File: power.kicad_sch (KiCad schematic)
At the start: 40 parts, among them T1 net-tie, U2 TPS546D24ARVFR

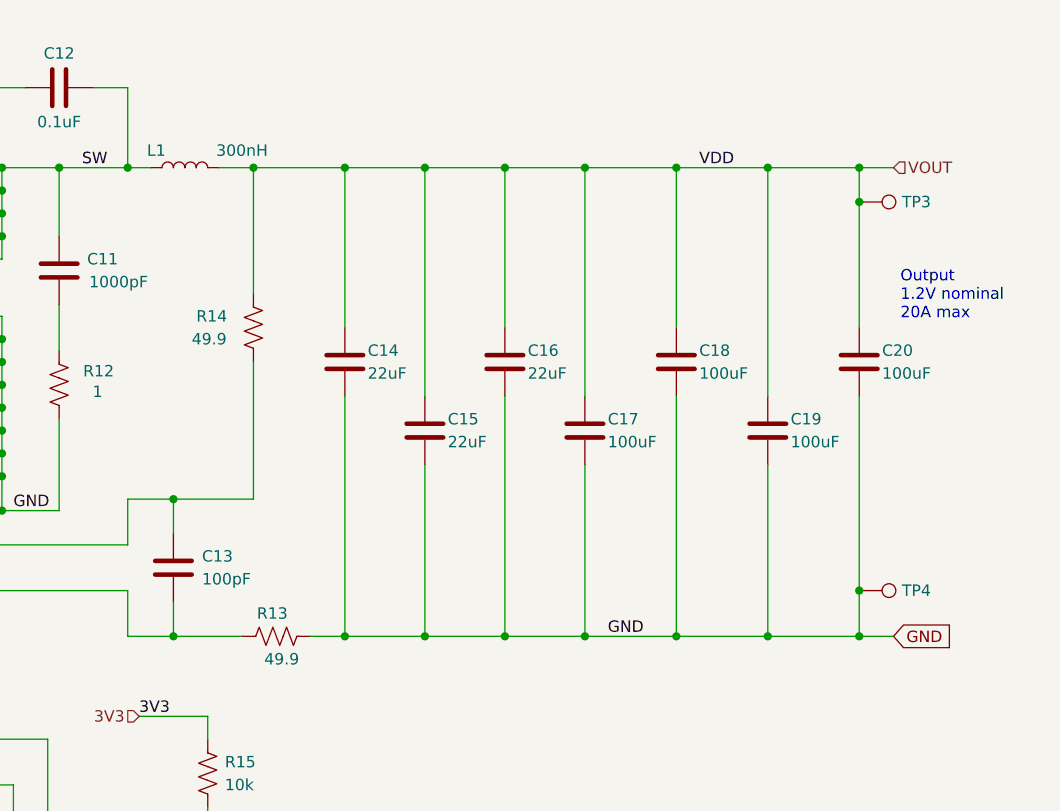
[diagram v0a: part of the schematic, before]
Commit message: use global GND level provided by default with KiCad and remove custom global GND
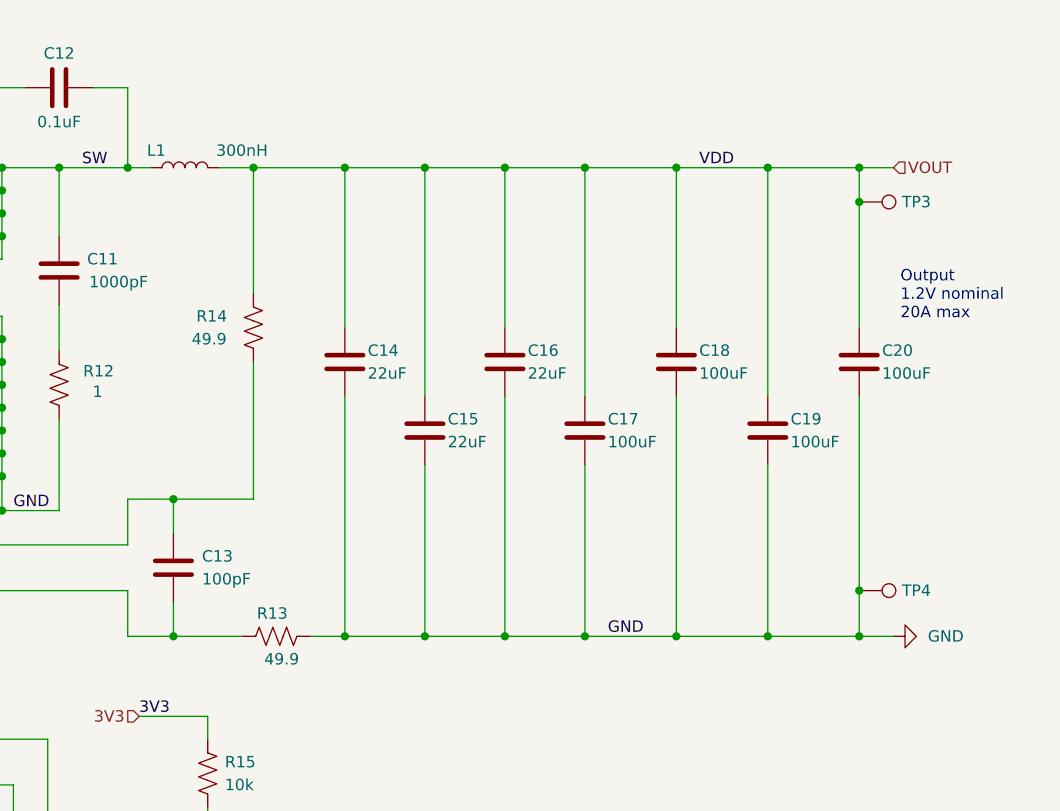
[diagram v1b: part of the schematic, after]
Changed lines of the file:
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@@
 (kicad_sch
-	(version 20231120)
+	(version 20250114)
 	(generator "eeschema")
-	(generator_version "8.0")
+	(generator_version "9.0")
 	(paper "A")
 	(title_block
@@
 		(rev "207")
 	)
+	(text "TPS546D24A is a Buck regulator that steps 4.5-5.5V down to 1.2V @ 20A for the BM1368"
+		(exclude_from_sim no)
+		(at 111.76 17.78 0)
+		(effects
+			(font
+				(size 1.27 1.27)
+			)
+			(justify left bottom)
+		)
+	)
+	(text "https://webench.ti.com/appinfo/webench/scripts/SDP.cgi?ID=3808DBEB40D18F5D"
+		(exclude_from_sim no)
+		(at 152.908 19.304 0)
+		(effects
+			(font
+				(size 1.27 1.27)
+			)
+		)
+	)
+	(text "Input \n4.5-5.5V"
+		(exclude_from_sim no)
+		(at 25.908 28.448 0)
+		(effects
+			(font
+				(size 1.27 1.27)
+			)
+			(justify left bottom)
+		)
+	)
+	(text "PGD is an open drain output\nfrom the TPS546D24. Pull up to 3.3V"
+		(exclude_from_sim no)
+		(at 151.13 120.65 0)
+		(effects
+			(font
+				(size 1.27 1.27)
+			)
+			(justify left bottom)
+		)
+	)
+	(text "I2C ADDR = 0x24"
+		(exclude_from_sim no)
+		(at 85.344 91.186 0)
+		(effects
+			(font
+				(size 1.27 1.27)
+			)
+			(justify left bottom)
+		)
+	)
+	(text "Output \n1.2V nominal\n20A max"
+		(exclude_from_sim no)
+		(at 239.522 56.388 0)
+		(effects
+			(font
+				(size 1.27 1.27)
+			)
+			(justify left bottom)
+		)
+	)
+	(text "Connect at\nU3 Pin 37"
+		(exclude_from_sim no)
+		(at 115.57 148.59 0)
+		(effects
+			(font
+				(size 1.27 1.27)
+			)
+			(justify left bottom)
+		)
+	)
 	(junction
 		(at 66.04 90.17)
@@
 		)
 	)
-	(text "TPS546D24A is a Buck regulator that steps 4.5-5.5V down to 1.2V @ 20A for the BM1368"
-		(exclude_from_sim no)
-		(at 111.76 17.78 0)
-		(effects
-			(font
-				(size 1.27 1.27)
-			)
-			(justify left bottom)
-		)
-	)
-	(text "https://webench.ti.com/appinfo/webench/scripts/SDP.cgi?ID=3808DBEB40D18F5D"
-		(exclude_from_sim no)
-		(at 152.908 19.304 0)
-		(effects
-			(font
-				(size 1.27 1.27)
-			)
-		)
-	)
-	(text "Input \n4.5-5.5V"
-		(exclude_from_sim no)
-		(at 25.908 28.448 0)
-		(effects
-			(font
-				(size 1.27 1.27)
-			)
-			(justify left bottom)
-		)
-	)
-	(text "PGD is an open drain output\nfrom the TPS546D24. Pull up to 3.3V"
-		(exclude_from_sim no)
-		(at 151.13 120.65 0)
-		(effects
-			(font
-				(size 1.27 1.27)
-			)
-			(justify left bottom)
-		)
-	)
-	(text "I2C ADDR = 0x24"
-		(exclude_from_sim no)
-		(at 85.344 91.186 0)
-		(effects
-			(font
-				(size 1.27 1.27)
-			)
-			(justify left bottom)
-		)
-	)
-	(text "Output \n1.2V nominal\n20A max"
-		(exclude_from_sim no)
-		(at 239.522 56.388 0)
-		(effects
-			(font
-				(size 1.27 1.27)
-			)
-			(justify left bottom)
-		)
-	)
-	(text "Connect at\nU3 Pin 37"
-		(exclude_from_sim no)
-		(at 115.57 148.59 0)
-		(effects
-			(font
-				(size 1.27 1.27)
-			)
-			(justify left bottom)
-		)
-	)
 	(label "GND"
 		(at 134.62 140.97 180)
-		(fields_autoplaced yes)
 		(effects
 			(font
@@
 	(label "PMB_SDA"
 		(at 99.06 101.6 0)
-		(fields_autoplaced yes)
 		(effects
 			(font
@@
 	(label "GND"
 		(at 96.52 74.93 0)
-		(fields_autoplaced yes)
 		(effects
 			(font
@@
 	(label "SW"
 		(at 148.59 39.37 0)
-		(fields_autoplaced yes)
 		(effects
 			(font
@@
 	(label "GND"
 		(at 140.97 77.47 0)
-		(fields_autoplaced yes)
 		(effects
 			(font
@@
 	(label "PMB_SCL"
 		(at 99.06 104.14 0)
-		(fields_autoplaced yes)
 		(effects
 			(font
@@
 	(label "AGND"
 		(at 118.11 128.27 180)
-		(fields_autoplaced yes)
 		(effects
 			(font
@@
 	(label "AGND"
 		(at 72.39 72.39 0)
-		(fields_autoplaced yes)
 		(effects
 			(font
@@
 	(label "GND"
 		(at 207.01 91.44 0)
-		(fields_autoplaced yes)
 		(effects
 			(font
@@
 	(label "PMB_ALRT"
 		(at 99.06 106.68 0)
-		(fields_autoplaced yes)
 		(effects
 			(font
@@
 	(label "PGOOD"
 		(at 147.32 114.3 0)
-		(fields_autoplaced yes)
 		(effects
 			(font
@@
 	(label "GND"
 		(at 63.5 34.29 0)
-		(fields_autoplaced yes)
 		(effects
 			(font
@@
 	(label "AGND"
 		(at 109.22 140.97 0)
-		(fields_autoplaced yes)
 		(effects
 			(font
@@
 	(label "VIN"
 		(at 35.56 17.78 0)
-		(fields_autoplaced yes)
 		(effects
 			(font
@@
 	(label "VDD"
 		(at 217.17 39.37 0)
-		(fields_autoplaced yes)
 		(effects
 			(font
@@
 	(label "3V3"
 		(at 154.94 100.33 0)
-		(fields_autoplaced yes)
 		(effects
 			(font
@@
 		)
 	)
-	(global_label "GND"
-		(shape input)
-		(at 238.76 91.44 0)
-		(fields_autoplaced yes)
-		(effects
-			(font
-				(size 1.27 1.27)
-			)
-			(justify left)
-		)
-		(property "Intersheetrefs" "${INTERSHEET_REFS}"
-			(at 245.6157 91.44 0)
-			(effects
-				(font
-					(size 1.27 1.27)
-				)
-				(justify left)
-				(hide yes)
-			)
-		)
-	)
 	(hierarchical_label "VOUT"
 		(shape input)
 		(at 238.76 39.37 0)
-		(fields_autoplaced yes)
 		(effects
 			(font
@@
 		(shape output)
 		(at 99.06 106.68 180)
-		(fields_autoplaced yes)
 		(effects
 			(font
@@
 		(shape input)
 		(at 154.94 100.33 180)
-		(fields_autoplaced yes)
 		(effects
 			(font
@@
 		(shape input)
 		(at 99.06 104.14 180)
-		(fields_autoplaced yes)
 		(effects
 			(font
@@
 		(shape output)
 		(at 172.72 114.3 0)
-		(fields_autoplaced yes)
 		(effects
 			(font
@@
 		(shape input)
 		(at 99.06 101.6 180)
-		(fields_autoplaced yes)
 		(effects
 			(font
@@
 		(shape output)
 		(at 102.87 17.78 0)
-		(fields_autoplaced yes)
 		(effects
 			(font
@@
 		(shape input)
 		(at 34.29 17.78 180)
-		(fields_autoplaced yes)
 		(effects
 			(font
@@
 	)
 	(symbol
+		(lib_id "power:GND")
+		(at 238.76 91.44 90)
+		(mirror x)
+		(unit 1)
+		(exclude_from_sim no)
+		(in_bom yes)
+		(on_board yes)
+		(dnp no)
+		(property "Reference" "#PWR04"
+			(at 245.11 91.44 0)
+			(effects
+				(font
+					(size 1.27 1.27)
+				)
+				(hide yes)
+			)
+		)
+		(property "Value" "GND"
+			(at 242.57 91.4399 90)
+			(effects
+				(font
+					(size 1.27 1.27)
+				)
+				(justify right)
+			)
+		)
+		(property "Footprint" ""
+			(at 238.76 91.44 0)
+			(effects
+				(font
+					(size 1.27 1.27)
+				)
+				(hide yes)
+			)
+		)
+		(property "Datasheet" ""
+			(at 238.76 91.44 0)
+			(effects
+				(font
+					(size 1.27 1.27)
+				)
+				(hide yes)
+			)
+		)
+		(property "Description" "Power symbol creates a global label with name \"GND\" , ground"
+			(at 238.76 91.44 0)
+			(effects
+				(font
+					(size 1.27 1.27)
+				)
+				(hide yes)
+			)
+		)
+		(pin "1"
+		)
+		(instances
+			(project "bitaxeUltra"
+				(path "/e63e39d7-6ac0-4ffd-8aa3-1841a4541b55/8ec0a9c6-2b78-44ef-a83d-9047d2828409"
+					(reference "#PWR04")
+					(unit 1)
+				)
+			)
+		)
+	)
+	(symbol
 		(lib_id "Device:R_US")
 		(at 92.71 49.53 0)
@@
 		)
 	)
+	(embedded_fonts no)
 )
